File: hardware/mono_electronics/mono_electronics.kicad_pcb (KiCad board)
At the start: 4 copper layers, 190 x 148 mm, 173 parts, among them SW1 KMR2, U1 ESP32-S3FN8, Y1 L327S400H11L

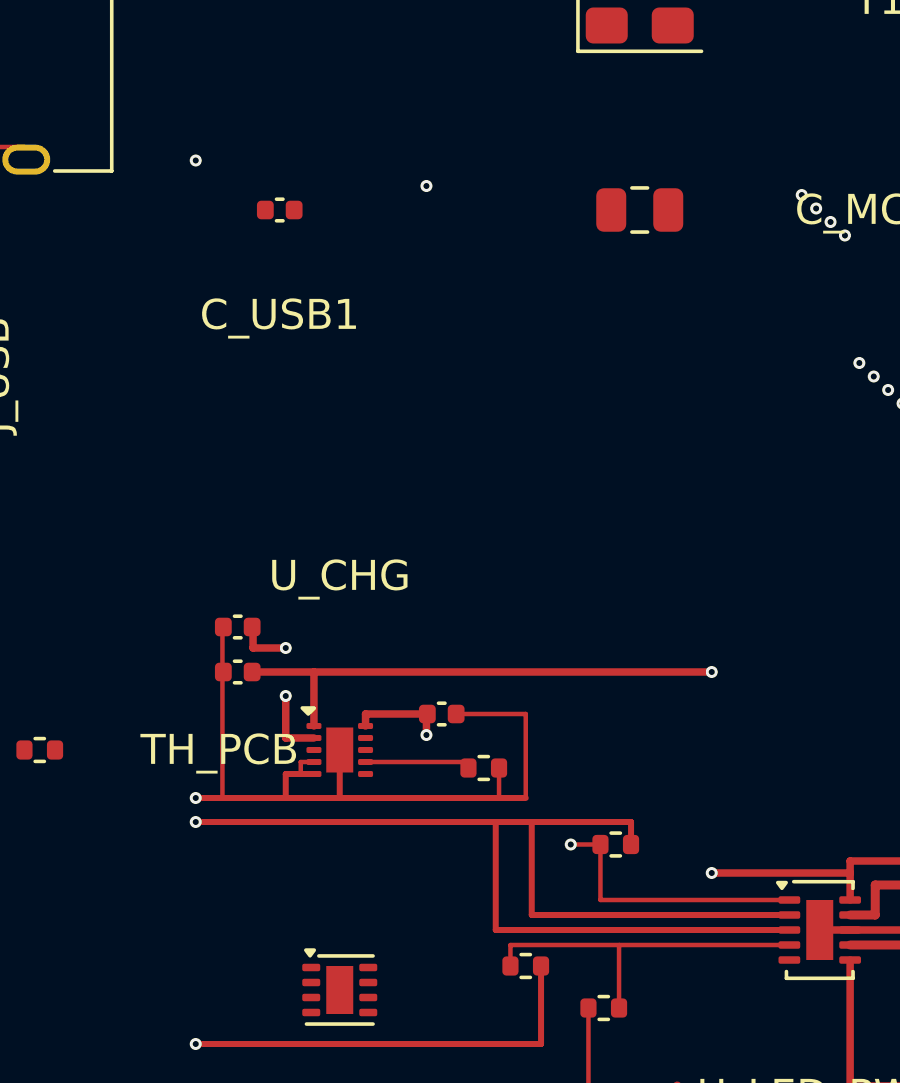
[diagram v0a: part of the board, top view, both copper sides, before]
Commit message: Use 0805 10 µF capacitors beside the charger pins.
The 0402 1 µF parts cannot hold the datasheet capacitance on the 5 V input and system rails after DC bias.

Co-authored-by: illiapliukhin <illiapliukhin@users.noreply.github.com>
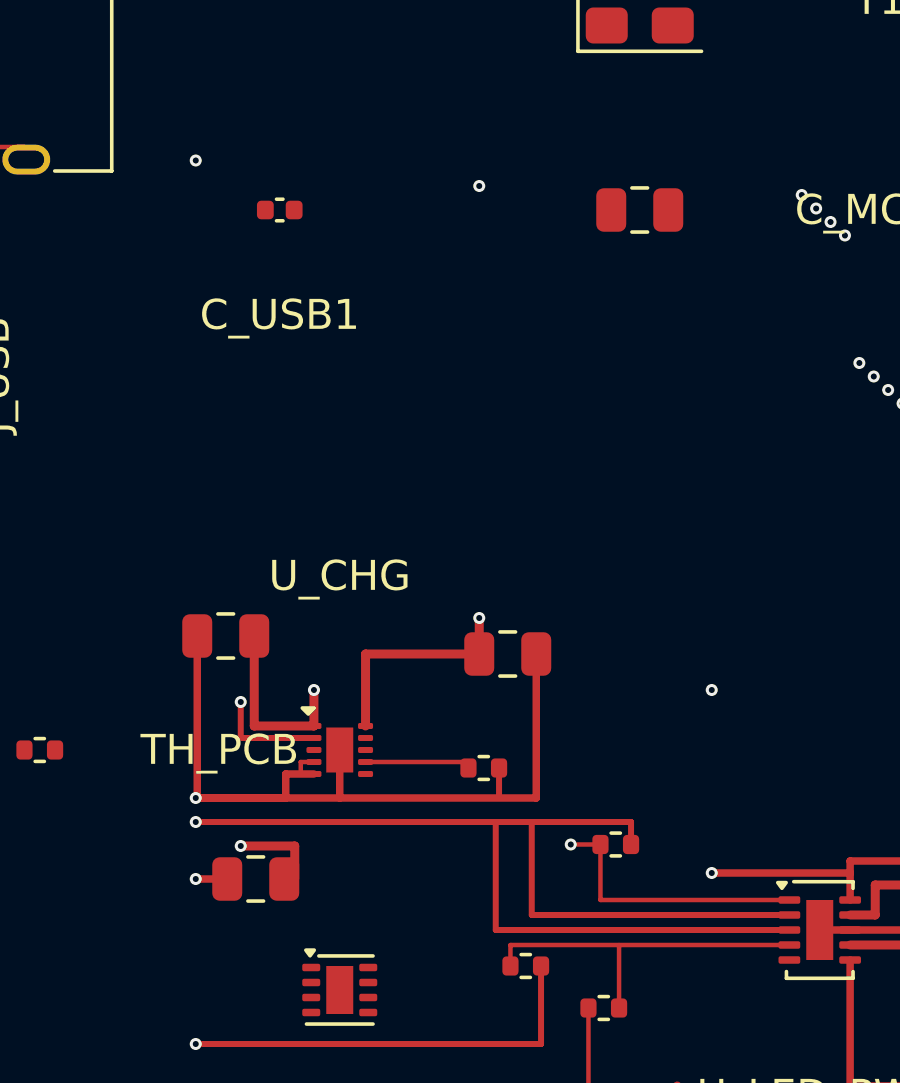
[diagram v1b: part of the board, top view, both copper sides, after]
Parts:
- removed the C_CHG_BAT at (14.6, 37.9)
- removed the C_CHG_IN at (21.4, 40.8)
- removed the C_CHG_SYS at (14.6, 39.4)
- added C_CHG_BAT: 10u, C_0805_2012Metric, F.Cu at (15.2, 46.3)
- added C_CHG_IN: 10u, C_0805_2012Metric, F.Cu at (23.6, 38.8)
- added C_CHG_SYS: 10u, C_0805_2012Metric, F.Cu at (14.2, 38.2)
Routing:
- net BAT_RAW: track 5.73 -> 11.3 mm
- net VBUS: track 47.9 -> 50.0 mm
- net SYS: track 62.8 -> 64.6 mm, vias 3 -> 4
- net GND: track 901.8 -> 902.6 mm, vias 46 -> 47

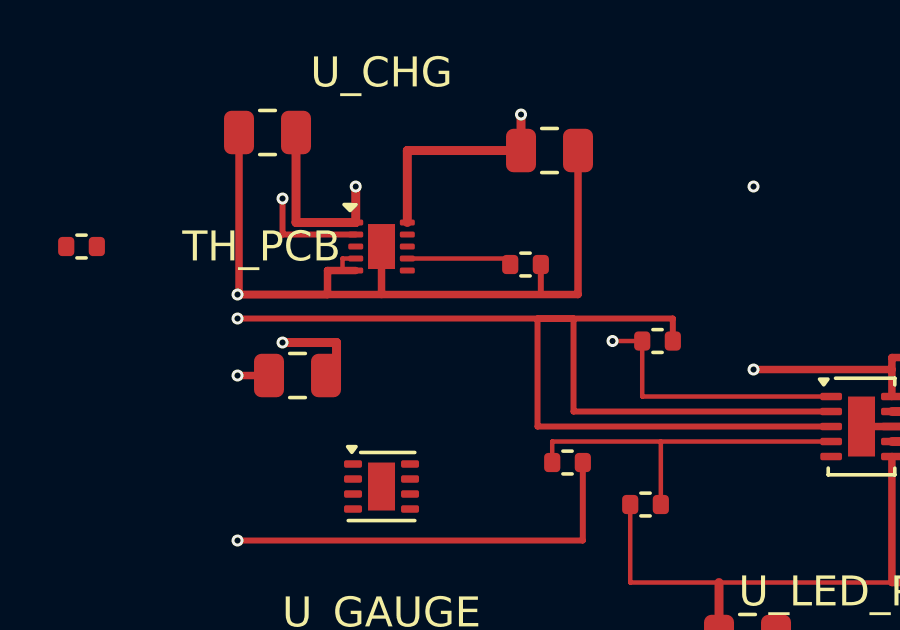
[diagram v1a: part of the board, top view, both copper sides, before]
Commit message: Hold the charger TS pin at the 10 kΩ thermistor bias.
BQ25185 suspends charge while TS/MR is open. A 10 kΩ resistor to GND is the datasheet 25°C point for the 10 kΩ β3435 pack thermistor.

Co-authored-by: illiapliukhin <illiapliukhin@users.noreply.github.com>
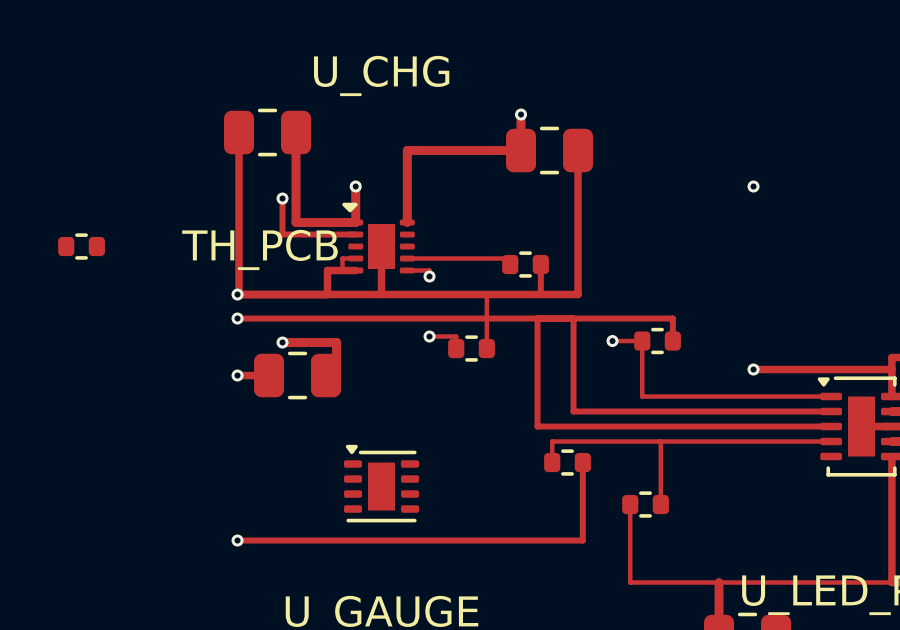
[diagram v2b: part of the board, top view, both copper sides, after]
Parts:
- added R_TS: 10k, R_0402_1005Metric, F.Cu at (21.0, 45.4)
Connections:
- U_CHG pad 6: (no net) -> TS_MR
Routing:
- net TS_MR: track 0.00 -> 4.23 mm, vias 0 -> 2
- net GND: track 902.6 -> 904.4 mm

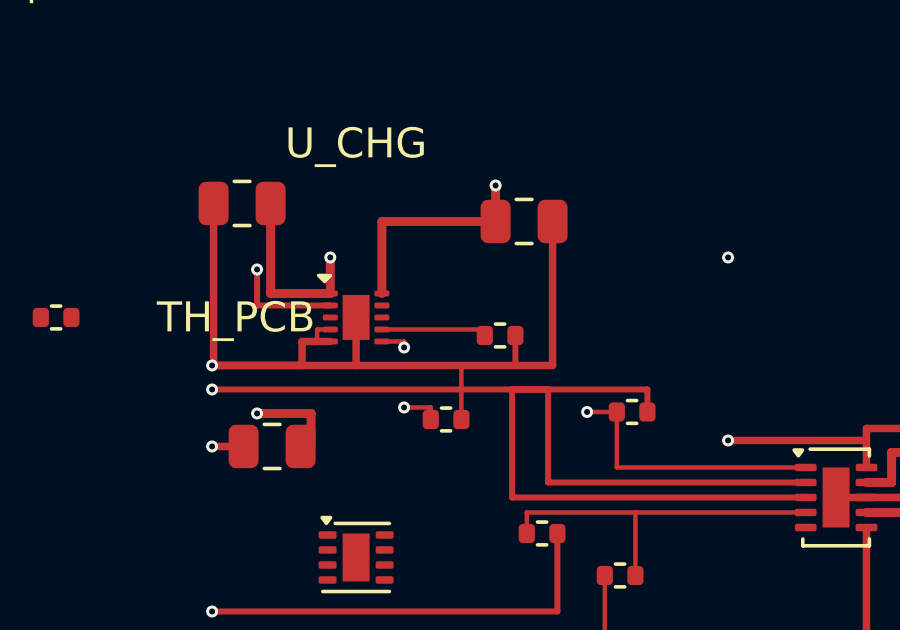
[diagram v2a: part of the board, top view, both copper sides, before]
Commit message: Set the charger for a 1000-1500 mAh cell.
18 kΩ on ILIM/VSET is 4.2 V and a 500 mA input limit. 600 Ω on ISET is 500 mA of charge, which is 0.5C at 1000 mAh and 0.33C at 1500 mAh.

Co-authored-by: illiapliukhin <illiapliukhin@users.noreply.github.com>
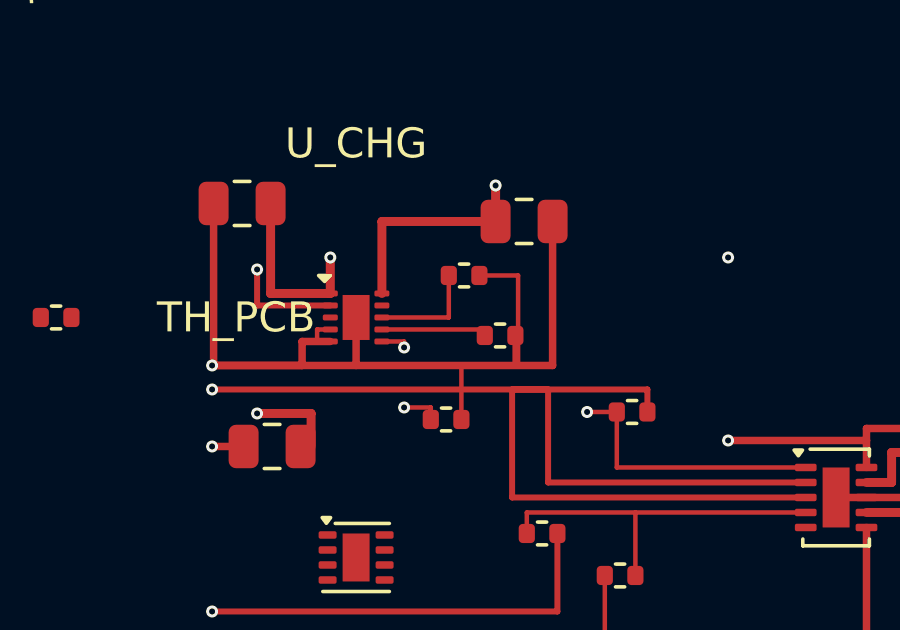
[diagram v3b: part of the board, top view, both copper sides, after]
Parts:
- added R_ISET: 600R, R_0402_1005Metric, F.Cu at (21.6, 40.6)
- R_ILIM: value 24k -> 18k
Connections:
- U_CHG pad 8: (no net) -> ISET
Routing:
- net GND: track 904.4 -> 908.7 mm
- net ISET: track 0.00 -> 3.63 mm

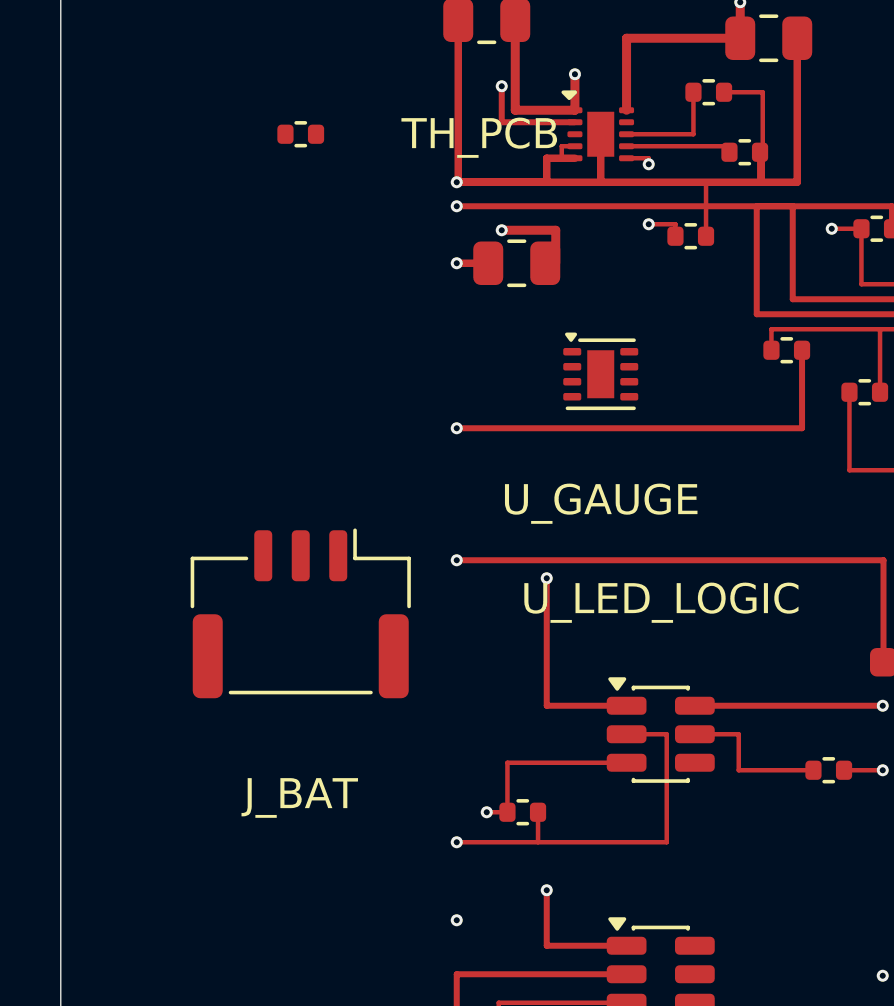
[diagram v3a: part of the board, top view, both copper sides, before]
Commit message: Wire Jauch LP523450JU onto the PicoBlade battery header.
The pack uses Molex 51021-0300, so J_BAT is now 53398-0371: pin 1 BAT+, pin 2 NTC, pin 3 GND. The onboard 10 kΩ no longer sits in parallel with the pack thermistor.

Co-authored-by: illiapliukhin <illiapliukhin@users.noreply.github.com>
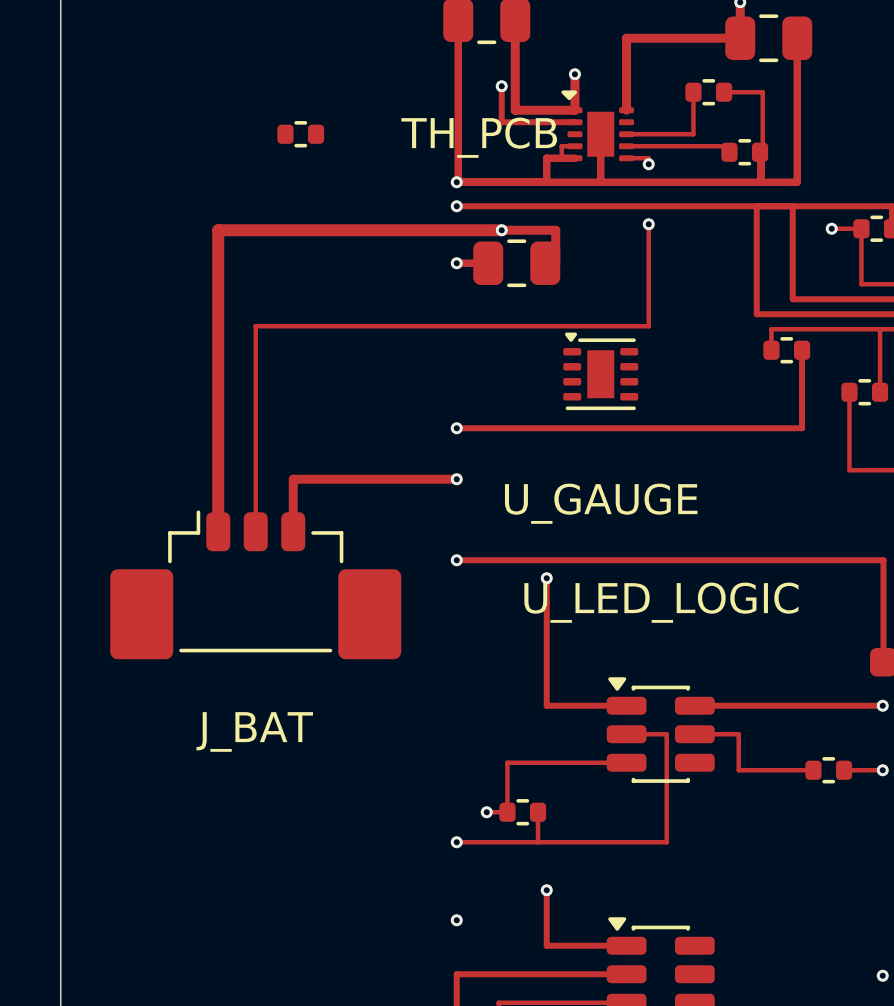
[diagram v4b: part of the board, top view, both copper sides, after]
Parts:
- removed the J_BAT at (8.00, 58.0)
- removed R_TS: 10k, R_0402_1005Metric
- added J_BAT: 53398-0371, Molex_PicoBlade_53398-0371_1x03-1MP_P1.25mm_Vertical, F.Cu at (6.50, 56.5)
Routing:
- net TS_MR: track 4.23 -> 26.3 mm
- net BAT_RAW: track 11.3 -> 30.8 mm
- net GND: track 908.7 -> 914.1 mm, vias 47 -> 48

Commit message: Turn the battery header to match the Jauch wire order.
The pack drawing puts black on top and red on the bottom. J_BAT is rotated so pin 3, pin 2, and pin 1 follow that order.

Co-authored-by: illiapliukhin <illiapliukhin@users.noreply.github.com>
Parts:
- moved J_BAT 1.53 mm to (6.80, 58.0), turned to 90 degrees
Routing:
- net BAT_RAW: track 30.8 -> 40.2 mm
- net TS_MR: track 26.3 -> 34.3 mm
- net GND: track 914.1 -> 918.2 mm

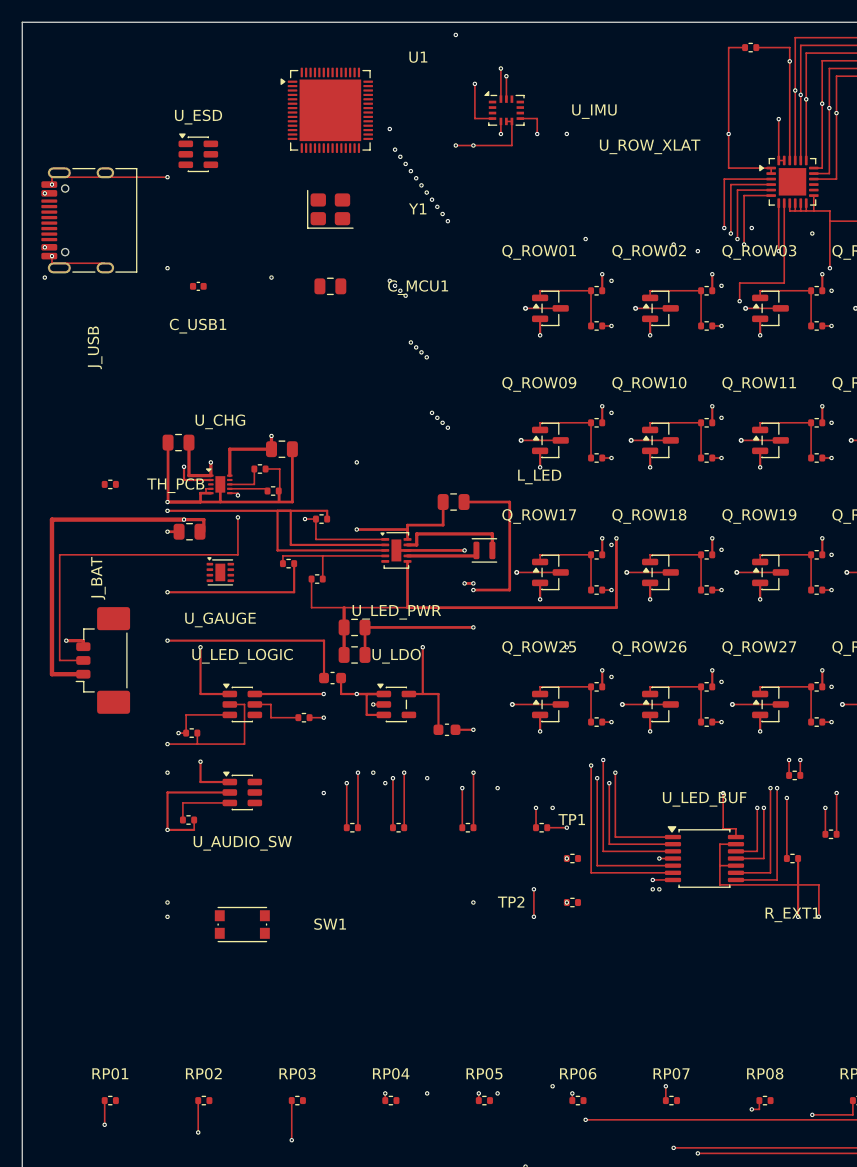
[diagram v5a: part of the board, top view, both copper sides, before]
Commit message: Complete mono electronics ESP32-S3 GPIO assignment and routing
Add mono_split_esp32 module to map FN8 pads, join existing row/LED reserve
spines, route IMU/USB/crystal/straps, and document the EVT pin table.
Regenerate mono PCBs; LED panels remain DRC-clean.

Co-authored-by: illiapliukhin <illiapliukhin@users.noreply.github.com>
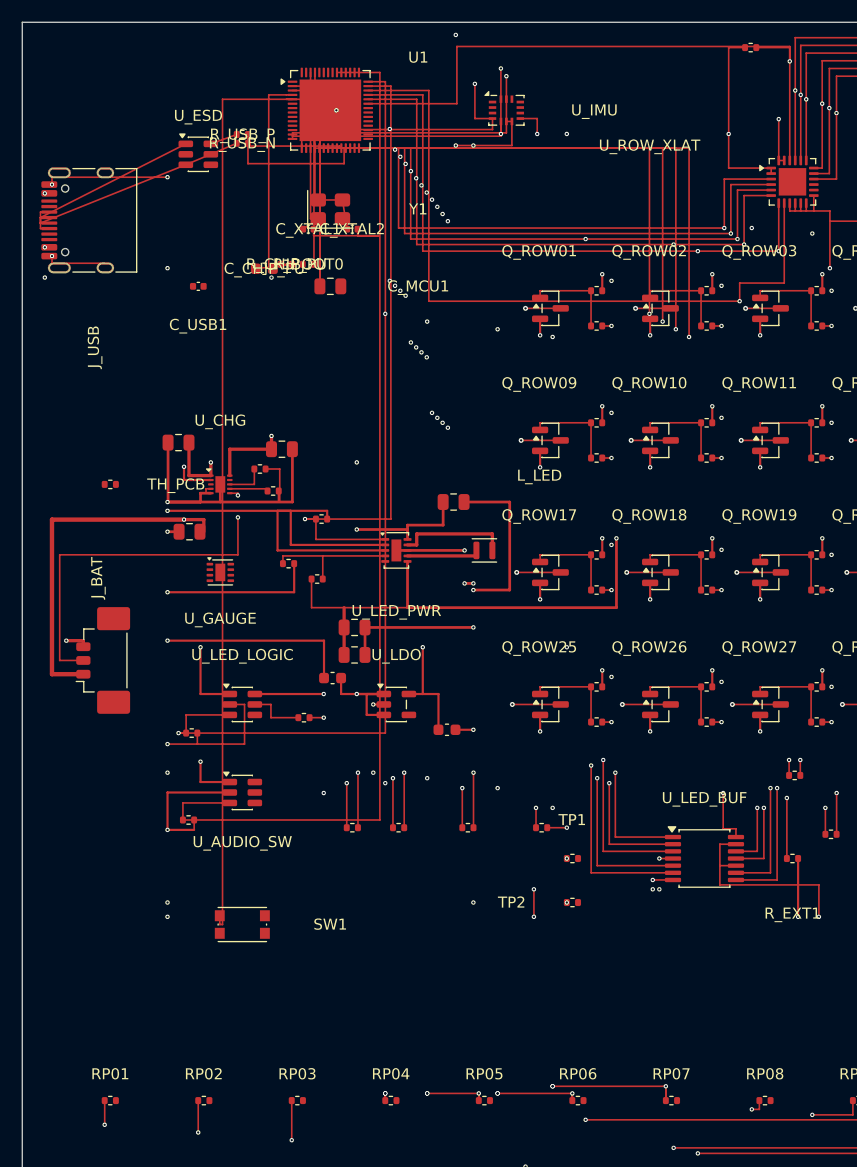
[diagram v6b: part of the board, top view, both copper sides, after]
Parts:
- added C_CHIP_PU: 1u, C_0603_1608Metric, F.Cu at (22.0, 22.4)
- added C_XTAL1: 10p, C_0402_1005Metric, F.Cu at (26.0, 18.8)
- added C_XTAL2: 10p, C_0402_1005Metric, F.Cu at (30.0, 18.8)
- added R_BOOT0: 10k, R_0402_1005Metric, F.Cu at (26.0, 22.0)
- added R_CHIP_PU: 10k, R_0402_1005Metric, F.Cu at (24.0, 22.0)
- added R_USB_N: 22R, R_0402_1005Metric, F.Cu at (20.0, 11.0)
- added R_USB_P: 22R, R_0402_1005Metric, F.Cu at (20.0, 10.2)
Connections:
- C_MCU1 pad 1: (no net) -> AON_3V3
- C_MCU1 pad 2: (no net) -> GND
- C_USB1 pad 1: (no net) -> VBUS
- C_USB1 pad 2: (no net) -> GND
- J_USB pad A6: (no net) -> USB_D_P
- J_USB pad A7: (no net) -> USB_D_N
- J_USB pad B6: (no net) -> USB_D_P
- J_USB pad B7: (no net) -> USB_D_N
- SW1 pad 1: (no net) -> GPIO0_BOOT
- SW1 pad 2: (no net) -> GND
- U1 pad 11: (no net) -> GND
- U1 pad 13: (no net) -> IMU_SDA
- U1 pad 14: (no net) -> IMU_SCL
- U1 pad 15: (no net) -> IMU_INT1
- U1 pad 18: (no net) -> LED_CLK
- U1 pad 19: (no net) -> LED_SDI
- U1 pad 2: (no net) -> AON_3V3
- U1 pad 20: (no net) -> AON_3V3
- U1 pad 21: (no net) -> LED_LE
- U1 pad 22: (no net) -> LED_OE_N
- U1 pad 23: (no net) -> ROW_A0
- U1 pad 24: (no net) -> ROW_A1
- U1 pad 25: (no net) -> USB_D_N_MCU
- U1 pad 26: (no net) -> USB_D_P_MCU
- U1 pad 27: (no net) -> ROW_A2
- U1 pad 29: (no net) -> AON_3V3
- U1 pad 3: (no net) -> AON_3V3
- U1 pad 32: (no net) -> GND
- U1 pad 37: (no net) -> ROW_XLAT_OE_N
- U1 pad 38: (no net) -> ROW_A3
- U1 pad 39: (no net) -> DEC_A_EN_N
- U1 pad 4: (no net) -> CHIP_PU
- U1 pad 40: (no net) -> DEC_B_EN_N
- U1 pad 41: (no net) -> LED_EN
- U1 pad 42: (no net) -> LED_LOGIC_EN
- U1 pad 44: (no net) -> GND
- U1 pad 45: (no net) -> GND
- U1 pad 46: (no net) -> AON_3V3
- U1 pad 48: (no net) -> AUDIO_EN
- U1 pad 5: (no net) -> GPIO0_BOOT
- U1 pad 53: (no net) -> XTAL_N
- U1 pad 54: (no net) -> XTAL_P
- U1 pad 55: (no net) -> AON_3V3
- U1 pad 56: (no net) -> AON_3V3
- U1 pad 57: (no net) -> GND
- U_ESD pad 1: (no net) -> USB_D_P
- U_ESD pad 2: (no net) -> GND
- U_ESD pad 3: (no net) -> USB_D_N
- U_ESD pad 4: (no net) -> GND
- U_ESD pad 5: (no net) -> GND
- U_ESD pad 6: (no net) -> USB_D_P
- Y1 pad 1: (no net) -> XTAL_P
- Y1 pad 2: (no net) -> GND
- Y1 pad 3: (no net) -> XTAL_N
- Y1 pad 4: (no net) -> GND
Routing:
- net LED_SDI: track 71.9 -> 215.7 mm, vias 5 -> 8
- net LED_OE_N: track 64.7 -> 206.3 mm, vias 5 -> 8
- net LED_LE: track 77.6 -> 218.8 mm, vias 5 -> 8
- net LED_CLK: track 68.1 -> 209.1 mm, vias 4 -> 7
- net GPIO0_BOOT: track 0.00 -> 99.9 mm
- net AUDIO_EN: track 5.81 -> 95.5 mm
- net LED_LOGIC_EN: track 206.1 -> 285.7 mm
- net DEC_B_EN_N: track 160.3 -> 213.2 mm
- net DEC_A_EN_N: track 138.1 -> 189.6 mm
- net LED_EN: track 207.2 -> 256.4 mm
- net ROW_A3: track 133.0 -> 180.4 mm
- net ROW_XLAT_OE_N: track 156.0 -> 200.9 mm
- net ROW_A1: track 100.6 -> 143.8 mm
- net ROW_A2: track 135.9 -> 179.0 mm
- net ROW_A0: track 92.8 -> 135.3 mm
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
